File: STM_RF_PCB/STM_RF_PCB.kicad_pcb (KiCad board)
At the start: 4 copper layers, 46 parts, among them J1 SMA, J2 USB_B_Micro, J3 SWD STLINk, J4 Conn_01x04, SW1 UP, SW2 LF, SW3 DN, SW4 RT, SW5 A, SW6 B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

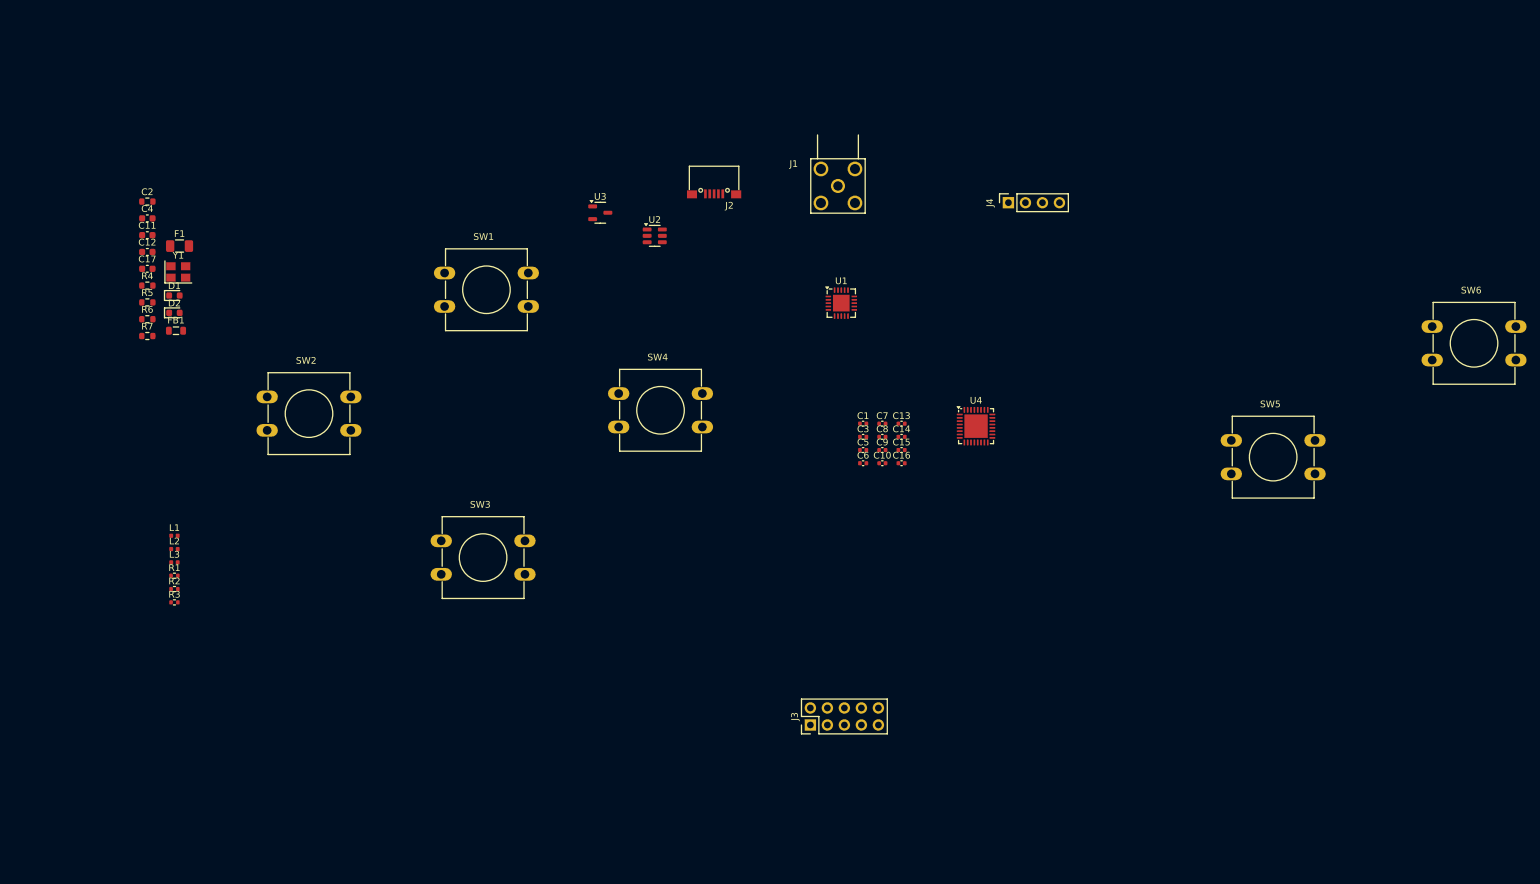
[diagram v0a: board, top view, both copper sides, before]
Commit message: Added start select buttons
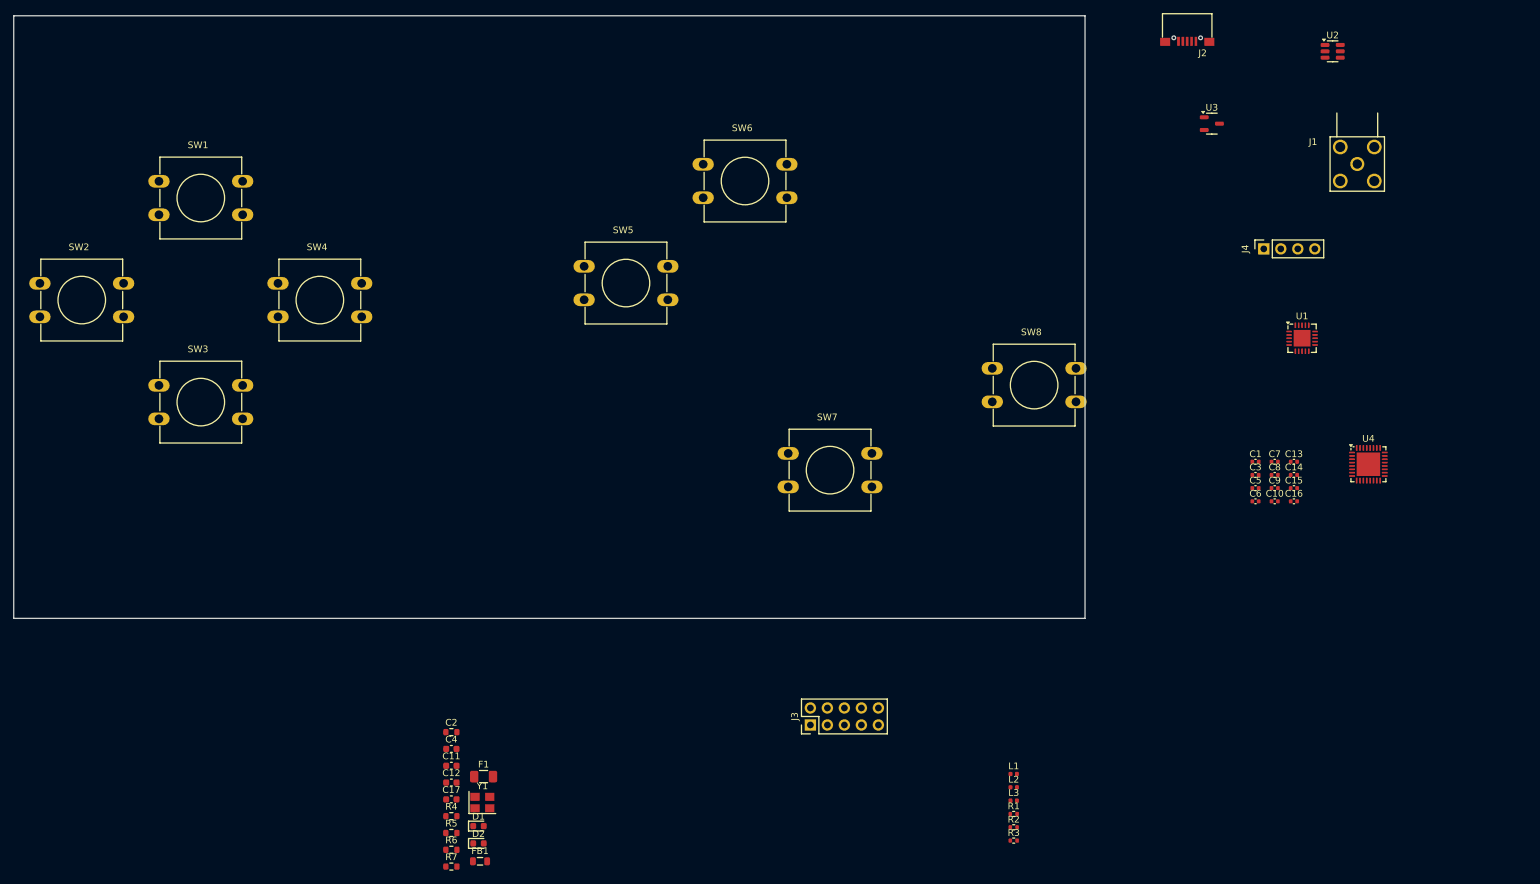
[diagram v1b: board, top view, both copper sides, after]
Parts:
- added SW7: A, Library:TC-1103-C-D, F.Cu at (141.1, 88.9)
- added SW8: B, Library:TC-1103-C-D, F.Cu at (171.6, 76.2)
- moved L3 130.3 mm to (174.8, 140.8)
- moved R3 130.3 mm to (174.8, 146.8)
- moved L1 130.3 mm to (174.8, 136.8)
- moved L2 130.3 mm to (174.8, 138.8)
- moved R1 130.3 mm to (174.8, 142.8)
- moved R2 130.3 mm to (174.8, 144.8)
- moved SW6 111.5 mm to (128.4, 45.8)
- moved U2 104.9 mm to (222.4, 28.9)
- moved SW5 100.1 mm to (110.6, 61.0)
- moved U3 92.3 mm to (204.3, 39.7)
- moved C11 91.3 mm to (90.8, 135.6)
- moved C12 91.3 mm to (90.8, 138.1)
- moved C17 91.3 mm to (90.8, 140.6)
- moved C2 91.3 mm to (90.8, 130.6)
- moved C4 91.3 mm to (90.8, 133.1)
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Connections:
- U4 pad 14: unconnected-(U4-PB0-Pad14) -> Button_SELECT
- U4 pad 15: unconnected-(U4-PB1-Pad15) -> Button_START
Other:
- board outline added: 160 x 90 mm

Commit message: PCB work
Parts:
- SW7: value A -> SELECT
- SW8: value B -> START
- moved C11 184.5 mm to (254.2, 50.0)
- moved C17 184.5 mm to (254.2, 55.0)
- moved C4 184.5 mm to (254.2, 47.5)
- moved R4 184.5 mm to (254.2, 57.5)
- moved R7 184.5 mm to (254.2, 65.0)
- moved C12 184.5 mm to (254.2, 52.5)
- moved C2 184.5 mm to (254.2, 45.0)
- moved R5 184.5 mm to (254.2, 60.0)
- moved R6 184.5 mm to (254.2, 62.5)
- moved D1 151.3 mm to (242.6, 112.2)
- moved D2 151.3 mm to (242.6, 114.8)
- moved F1 151.3 mm to (243.4, 104.8)
- moved FB1 151.3 mm to (242.8, 117.5)
- moved Y1 151.3 mm to (243.2, 108.7)
- moved R1 106.7 mm to (280.3, 158.6)
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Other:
- board text added: "Start Point: 68.5mm, 60mm End Point: 228.5mm,150mm Height 90mm Width 160mm"

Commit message: PCB work
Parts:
- moved U2 133.1 mm to (135.5, 74.5)
- moved U4 127.6 mm to (148.5, 105.0)
- moved J4 114.5 mm to (144.4, 84.5)
- moved U3 98.9 mm to (151.5, 76.5)
- moved U1 86.8 mm to (182.6, 80.0)
- moved R1 50.8 mm to (259.0, 112.5)
- moved L3 50.8 mm to (259.0, 110.5)
- moved R3 50.8 mm to (259.0, 116.5)
- moved L1 50.8 mm to (259.0, 106.5)
- moved L2 50.8 mm to (259.0, 108.5)
- moved R2 50.8 mm to (259.0, 114.5)
- moved J3 38.5 mm to (211.4, 144.3)
- moved SW1 11.1 mm to (90.2, 89.5)
- moved SW4 11.0 mm to (103.2, 102.5)
- moved SW5 6.95 mm to (189.2, 109.0)
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
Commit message: PCB work
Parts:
- U3: footprint Package_TO_SOT_SMD:SOT-23-3 -> Library:XC6206P332MR
- U4: value STM32L432KBUx -> STM32L432KBU6; footprint Package_DFN_QFN:UFQFPN-32-1EP_5x5mm_P0.5mm_EP3.5x3.5mm -> Library:STM32L432KBU6
- moved U2 13.6 mm to (148.5, 70.5)
- moved J4 2.02 mm to (144.1, 86.5)
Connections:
- U4 pad 10: Button_LF -> Button_RT
- U4 pad 11: Button_RT -> Button_LF
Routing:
- net Button_B: track 0.00 -> 80.1 mm, vias 0 -> 1
- net Button_LF: track 0.00 -> 73.4 mm
- net Button_DN: track 0.00 -> 62.8 mm, vias 0 -> 1
- net Button_UP: track 0.00 -> 60.9 mm
- net Button_A: track 0.00 -> 60.0 mm, vias 0 -> 1
- net Button_RT: track 0.00 -> 46.4 mm
- net Button_SELECT: track 0.00 -> 45.3 mm
- net Button_START: track 0.00 -> 44.4 mm
- added copper zone on In2.Cu, net +3V3
- added copper zone on B.Cu, net GND
- added copper zone on F.Cu, net GND
- added copper zone on In1.Cu, net GND
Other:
- outline, holes or cut-outs redrawn
- board text added: "JLCJLCJLCJLC"

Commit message: pcb work
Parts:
- moved R4 137.6 mm to (123.5, 100.5), turned to 90 degrees
- moved R5 133.7 mm to (125.5, 96.0)
- moved R3 115.3 mm to (145.0, 99.0)
- moved C12 115.2 mm to (140.3, 69.5)
- moved D2 113.7 mm to (129.5, 103.5)
- moved D1 113.5 mm to (129.8, 99.5)
- moved R6 108.7 mm to (149.3, 91.0)
- moved C11 108.6 mm to (148.5, 75.0)
- moved C14 107.0 mm to (158.5, 106.5)
- moved FB1 105.8 mm to (145.5, 76.0), turned to 90 degrees
- moved C15 103.6 mm to (162.5, 106.5)
- moved R7 103.5 mm to (154.0, 91.0)
- moved C16 100.2 mm to (166.5, 106.5)
- moved C17 98.3 mm to (170.5, 106.5)
- moved F1 96.1 mm to (150.0, 82.0)
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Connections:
- U2 pad 1: USB_CONN_D+ -> USB_CONN_D-
- U2 pad 3: USB_CONN_D- -> USB_CONN_D+
- U2 pad 4: USB_D- -> USB_D+
- U2 pad 6: USB_D+ -> USB_D-
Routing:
- net USB_D-: track 0.00 -> 43.6 mm
- net USB_D+: track 0.00 -> 43.5 mm
- net +5V: track 0.00 -> 21.4 mm
- net USB_CONN_D+: track 0.00 -> 8.76 mm
- net Net-(F1-Pad1): track 0.00 -> 6.36 mm
- net Net-(U3-VI): track 0.00 -> 4.64 mm
- net USB_CONN_D-: track 0.00 -> 4.29 mm
- net GND: track 0.00 -> 3.48 mm, vias 0 -> 1
- net +3V3: track 0.00 -> 1.88 mm, vias 0 -> 1

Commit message: PCB work
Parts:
- moved C17 29.6 mm to (141.5, 100.7), turned to 90 degrees
- moved C13 27.0 mm to (194.5, 138.0), turned to 90 degrees
- moved J3 27.0 mm to (184.4, 144.3)
- moved C16 26.7 mm to (140.0, 103.5), turned to 180 degrees
- moved FB1 9.71 mm to (136.0, 78.0)
- moved F1 8.28 mm to (146.5, 74.5)
- moved C15 7.52 mm to (155.0, 107.0)
- moved C11 7.16 mm to (141.5, 73.5)
- moved U3 6.80 mm to (135.5, 73.0)
- moved C14 6.08 mm to (152.5, 107.5), turned to -90 degrees
- moved R5 4.53 mm to (126.0, 100.5), turned to 180 degrees
- moved R4 4.30 mm to (126.0, 104.0), turned to 180 degrees
- moved R3 2.23 mm to (147.0, 98.0), turned to 90 degrees
- moved R6 1.71 mm to (148.5, 92.5), turned to 90 degrees
- moved R7 1.58 mm to (153.5, 92.5), turned to 90 degrees
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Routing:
- net NRST: track 0.00 -> 70.5 mm, vias 0 -> 1
- net +3V3: track 1.88 -> 30.5 mm, vias 1 -> 3
- net I2C1_SCL: track 0.00 -> 27.4 mm, vias 0 -> 1
- net I2C1_SDA: track 0.00 -> 25.5 mm, vias 0 -> 1
- net Net-(D1-A): track 0.00 -> 18.0 mm
- net Net-(D2-A): track 0.00 -> 16.6 mm
- net +5V: track 21.4 -> 5.77 mm
- net Net-(F1-Pad1): track 6.36 -> 0.00 mm
- net Net-(U3-VI): track 4.64 -> 0.00 mm
- net Net-(D1-K): track 0.00 -> 4.26 mm
- net Net-(D2-K): track 0.00 -> 4.21 mm
- net Net-(U4-PH3): track 0.00 -> 4.16 mm
- net GND: track 3.48 -> 7.23 mm, vias 1 -> 6

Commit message: PCB work
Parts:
- moved C1 17.2 mm to (191.2, 70.0), turned to 90 degrees
- moved C3 15.0 mm to (173.0, 71.0)
- moved Y1 14.1 mm to (192.8, 81.8), turned to 180 degrees
- moved C4 13.4 mm to (170.0, 74.5)
- moved C12 12.8 mm to (129.5, 76.5), turned to -90 degrees
- moved L1 12.4 mm to (199.8, 77.5), turned to -90 degrees
- moved C5 12.0 mm to (197.0, 81.0)
- moved C7 11.8 mm to (202.2, 78.0)
- moved U1 11.1 mm to (192.8, 75.5)
- moved R2 10.3 mm to (188.5, 82.0), turned to -90 degrees
- moved L2 9.62 mm to (198.0, 76.0), turned to -90 degrees
- moved L3 9.39 mm to (200.2, 75.5)
- moved C2 9.18 mm to (170.0, 79.0)
- moved C6 8.56 mm to (191.5, 86.5), turned to -90 degrees
- moved R1 8.26 mm to (196.2, 70.0), turned to 90 degrees
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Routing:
- net SWCLK: track 0.00 -> 58.0 mm, vias 0 -> 1
- net SWDIO: track 0.00 -> 55.4 mm, vias 0 -> 1
- net +3V3: track 30.5 -> 43.6 mm, vias 3 -> 5
- net NRF_XC1: track 0.00 -> 12.5 mm
- net NRF_VDD_PA: track 0.00 -> 9.45 mm
- net Net-(J1-In): track 0.00 -> 8.99 mm
- net NRF_XC2: track 0.00 -> 6.67 mm
- net Net-(U3-VI): track 0.00 -> 6.01 mm
- net GND: track 7.23 -> 13.0 mm, vias 6 -> 7
- net +5V: track 5.77 -> 11.5 mm
- net NRF_ANT_1: track 0.00 -> 5.48 mm
- net NRF_ANT_2: track 0.00 -> 5.08 mm
- net Net-(U1-IREF): track 0.00 -> 4.06 mm
- net Net-(U1-DVDD): track 0.00 -> 3.52 mm
- net Net-(F1-Pad1): track 0.00 -> 2.54 mm
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
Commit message: PCB work
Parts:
- moved C2 29.3 mm to (198.5, 72.0)
- moved C4 23.9 mm to (192.2, 65.8), turned to 90 degrees
- moved C3 18.0 mm to (188.0, 81.0), turned to -90 degrees
- moved R2 8.61 mm to (196.2, 85.8), turned to 180 degrees
- moved C11 4.81 mm to (133.2, 74.2)
- moved C12 4.81 mm to (124.8, 75.8)
- moved F1 4.81 mm to (141.8, 73.2)
- moved FB1 4.81 mm to (136.8, 73.2)
- moved U3 4.81 mm to (128.8, 73.8)
- moved C1 2.45 mm to (188.8, 70.2), turned to 180 degrees
- turned U2 to -90 degrees
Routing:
- net NRF_CE: track 0.00 -> 56.2 mm, vias 0 -> 2
- net SPI_CS: track 0.00 -> 54.9 mm, vias 0 -> 2
- net SPI_MOSI: track 0.00 -> 53.8 mm, vias 0 -> 2
- net SPI_MISO: track 0.00 -> 53.1 mm, vias 0 -> 2
- net SPI_SCK: track 0.00 -> 52.8 mm, vias 0 -> 2
- net NRF_IRQ: track 0.00 -> 52.2 mm, vias 0 -> 2
- net GND: track 13.0 -> 28.3 mm, vias 7 -> 8
- net +3V3: track 43.6 -> 55.8 mm, vias 5 -> 6
- net +5V: track 11.5 -> 21.8 mm, vias 0 -> 2
- net NRF_XC2: track 6.67 -> 13.8 mm
- net USB_CONN_D+: track 9.33 -> 3.76 mm, vias 2 -> 0
- net USB_D+: track 43.5 -> 39.3 mm
- net USB_D-: track 43.6 -> 39.4 mm
- net Net-(U1-DVDD): track 3.52 -> 5.56 mm
- net NRF_XC1: track 12.5 -> 11.1 mm
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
